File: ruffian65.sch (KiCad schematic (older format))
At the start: 23 parts

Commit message: wired differential
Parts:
- removed R? (x2): 22, symbol Device:R_Small
- removed U?: ATmega32U4-AU, Package_QFP:TQFP-44_10x10mm_P0.8mm, symbol MCU_Microchip_ATmega:ATmega32U4-AU
- added U1: ATmega32U4-MU, Package_DFN_QFN:QFN-44-1EP_7x7mm_P0.5mm_EP5.2x5.2mm, symbol MCU_Microchip_ATmega:ATmega32U4-MU
- C1, C2, C3, C4, C5, C7: footprint (none) -> Capacitor_SMD:C_0805_2012Metric_Pad1.18x1.45mm_HandSolder
- C6, C8: renamed from C?; footprint (none) -> Capacitor_SMD:C_0805_2012Metric_Pad1.18x1.45mm_HandSolder
- D70: renamed from D?; footprint Package_TO_SOT_SMD:SOT-143 -> random-keyboard-parts:SOT143B
- F1: renamed from F?; footprint (none) -> Fuse:Fuse_1206_3216Metric_Pad1.42x1.75mm_HandSolder
- J1: renamed from J?; footprint (none) -> random-keyboard-parts:Reset_Pretty-Mask
- R1: footprint (none) -> Resistor_SMD:R_0805_2012Metric_Pad1.20x1.40mm_HandSolder
- R2, R3, R4, R5, R6: renamed from R?; footprint (none) -> Resistor_SMD:R_0805_2012Metric_Pad1.20x1.40mm_HandSolder
- SW70: renamed from SW?; footprint (none) -> Button_Switch_SMD:SW_SPST_SKQG_WithStem
- USB1: renamed from USB?; footprint (none) -> Type-C:HRO-TYPE-C-31-M-12-HandSoldering
- Y1: renamed from Y?; footprint (none) -> Crystal:Crystal_SMD_3225-4Pin_3.2x2.5mm_HandSoldering
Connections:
- net +5V: now also U1.14 (VCC), U1.2 (UVCC), U1.34 (VCC), U1.7 (VBUS)
- net D+: now also U1.4 (D+)
- net D-: now also U1.3 (D-)
- net GND: now also U1.5 (UGND)
- net MISO: now also U1.11 (PB3)
- net MOSI: now also U1.10 (PB2)
- net RESET: now also U1.13 (~RESET)
- net SCK: now also U1.9 (PB1)
- net XTAL1: now also U1.17 (XTAL1)
- net XTAL2: now also U1.16 (XTAL2)
- net at R1.2: now also U1.33 (~HWB~/PE2)
- net at C7.1: now also U1.6 (UCAP)
- net DN: now reaches D70.3 (I/O2), R3.2, USB1.5 (DN2), USB1.7 (DN1)
- net DP: now reaches D70.2 (I/O1), R4.2, USB1.6 (DP1), USB1.8 (DP2)
- new net: U1.15 (GND), U1.23 (GND), U1.35 (GND), U1.43 (GND), U1.45 (GND)
- new net: U1.24 (AVCC), U1.44 (AVCC)
- new net col0: U1.28 (PB4)
- new net col1: U1.29 (PB5)
- new net col10: U1.21 (PD3)
- new net col11: U1.22 (PD5)
- new net col12: U1.25 (PD4)
- new net col13: U1.26 (PD6)
- new net col14: U1.27 (PD7)
- new net col2: U1.30 (PB6)
- new net col3: U1.31 (PC6)
- new net col4: U1.32 (PC7)
- new net col5: U1.37 (PF6)
- new net col6: U1.36 (PF7)
- new net col7: U1.8 (PB0)
- new net col8: U1.19 (PD1)
- new net col9: U1.20 (PD2)
- new net row0: U1.1 (PE6)
- new net row1: U1.38 (PF5)
- new net row2: U1.41 (PF0)
- new net row3: U1.40 (PF1)
- new net row4: U1.39 (PF4)

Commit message: wiring done?
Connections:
- net +5V: now also U1.24 (AVCC), U1.44 (AVCC)
- net GND: now also U1.15 (GND), U1.23 (GND), U1.35 (GND), U1.43 (GND), U1.45 (GND)
- net col0: now also U1.20 (PD2); no longer U1.28 (PB4)
- net col1: now also U1.21 (PD3); no longer U1.29 (PB5)
- net col10: now also U1.18 (PD0); no longer U1.21 (PD3)
- net col11: now also U1.41 (PF0); no longer U1.22 (PD5)
- net col2: now also U1.22 (PD5); no longer U1.30 (PB6)
- net col8: now also U1.28 (PB4); no longer U1.19 (PD1)
- net col9: now also U1.38 (PF5); no longer U1.20 (PD2)
- net row1: now also U1.39 (PF4); no longer U1.38 (PF5)
- net row2: now also U1.12 (PB7); no longer U1.41 (PF0)
- net row4: now also U1.19 (PD1); no longer U1.39 (PF4)
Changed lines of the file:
@@
 Wire Wire Line
 	10750 3400 11050 3400
-Text GLabel 10250 1700 2    50   Input ~ 0
+Text GLabel 10250 2700 2    50   Input ~ 0
 col0
 Wire Wire Line
@@
 Wire Wire Line
 	10250 1600 10800 1600
-Text GLabel 10250 1800 2    50   Input ~ 0
+Text GLabel 10250 2800 2    50   Input ~ 0
 col1
-Text GLabel 10250 1900 2    50   Input ~ 0
+Text GLabel 10250 3000 2    50   Input ~ 0
 col2
 Text GLabel 10250 2300 2    50   Input ~ 0
@@
 col3
 Text GLabel 10250 2600 2    50   Input ~ 0
-col8
-Text GLabel 10250 2700 2    50   Input ~ 0
+row4
+Text GLabel 10250 4000 2    50   Input ~ 0
 col9
-Text GLabel 10250 2800 2    50   Input ~ 0
+Text GLabel 10250 2500 2    50   Input ~ 0
 col10
-Text GLabel 10250 3000 2    50   Input ~ 0
+Text GLabel 10250 3700 2    50   Input ~ 0
 col11
 Text GLabel 10250 2900 2    50   Input ~ 0
@@
 Text GLabel 10250 3500 2    50   Input ~ 0
 row0
-Text GLabel 10250 4000 2    50   Input ~ 0
+Text GLabel 10250 3900 2    50   Input ~ 0
 row1
-Text GLabel 10250 3700 2    50   Input ~ 0
+Text GLabel 10250 2000 2    50   Input ~ 0
 row2
 Text GLabel 10250 3800 2    50   Input ~ 0
 row3
-Text GLabel 10250 3900 2    50   Input ~ 0
-row4
+Text GLabel 10250 1700 2    50   Input ~ 0
+col8
 Text GLabel 10250 4100 2    50   Input ~ 0
 col5
 Text GLabel 10250 4200 2    50   Input ~ 0
 col6
+Wire Wire Line
+	9150 4600 9550 4600
+Wire Wire Line
+	9550 1000 9650 1000
+Text GLabel 6450 3400 3    50   Input ~ 0
+DP
+Text GLabel 6450 3300 1    50   Input ~ 0
+DN
 $Comp
 L MCU_Microchip_ATmega:ATmega32U4-MU U1
-U 1 1 61957B02
+U 1 1 61B499E8
 P 9650 2800
 F 0 "U1" H 9650 911 50  0000 C CNN
@@
 	1    0    0    -1
 $EndComp
+Connection ~ 9550 1000
 Wire Wire Line
-	9150 4600 9550 4600
+	9750 1000 9650 1000
+Connection ~ 9650 1000
 Wire Wire Line
-	9550 1000 9650 1000
-Connection ~ 9550 1000
-Text GLabel 6450 3400 3    50   Input ~ 0
-DP
-Text GLabel 6450 3300 1    50   Input ~ 0
-DN
+	9650 4600 9550 4600
+Connection ~ 9550 4600
 $EndSCHEMATC

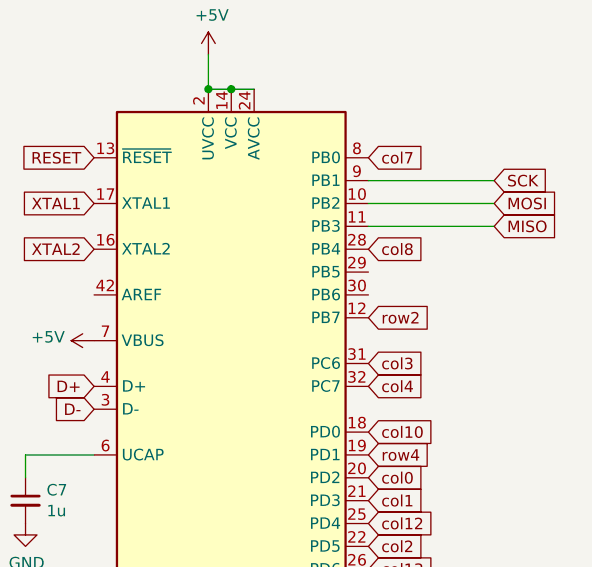
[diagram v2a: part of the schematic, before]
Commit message: added ec11
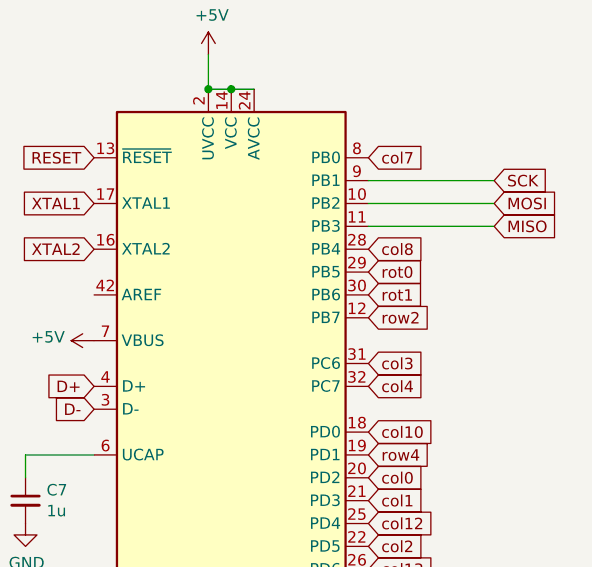
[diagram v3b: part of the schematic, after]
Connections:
- net rot0: now reaches U1.29 (PB5)
- net rot1: now reaches U1.30 (PB6)
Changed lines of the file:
@@
 	9650 4600 9550 4600
 Connection ~ 9550 4600
+Text GLabel 10250 1800 2    50   Input ~ 0
+rot0
+Text GLabel 10250 1900 2    50   Input ~ 0
+rot1
 $EndSCHEMATC

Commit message: encoder support?
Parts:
- removed USB1: HRO-TYPE-C-31-M-12, Type-C:HRO-TYPE-C-31-M-12-HandSoldering, symbol Type-C:HRO-TYPE-C-31-M-12
- added J2: USB_C_Receptacle_USB2.0, Connector_USB:USB_C_Receptacle_HRO_TYPE-C-31-M-12, symbol Connector:USB_C_Receptacle_USB2.0
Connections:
- net DN: now also J2.A7 (D-), J2.B7 (D-)
- net DP: now also J2.A6 (D+), J2.B6 (D+)
- net GND: now also J2.A1 (GND), J2.A12 (GND), J2.B1 (GND), J2.B12 (GND), J2.S1 (SHIELD)
- net VCC: now also J2.A4 (VBUS), J2.A9 (VBUS), J2.B4 (VBUS), J2.B9 (VBUS)
- net at R5.1: now also J2.B5 (CC2)
- net at R6.1: now also J2.A5 (CC1)
- no-connect marks 0 -> 2
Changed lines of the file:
@@
 	7200 1500 7200 1650
-$Comp
-L Type-C:HRO-TYPE-C-31-M-12 USB1
-U 1 1 6139D968
-P 5800 3250
-F 0 "USB1" H 5633 4047 60  0000 C CNN
-F 1 "HRO-TYPE-C-31-M-12" H 5633 3941 60  0000 C CNN
-F 2 "Type-C:HRO-TYPE-C-31-M-12-HandSoldering" H 5800 3250 60  0001 C CNN
-F 3 "" H 5800 3250 60  0001 C CNN
-	1    5800 3250
-	1    0    0    -1
-$EndComp
 $Comp
 L Device:R_Small R3
@@
 Wire Wire Line
 	7900 3400 8150 3400
-Wire Wire Line
-	5900 2700 6000 2700
-Wire Wire Line
-	6000 2700 6000 3800
-Wire Wire Line
-	6000 3800 5900 3800
-Wire Wire Line
-	5900 3900 6000 3900
-Wire Wire Line
-	6000 3900 6000 3800
-Connection ~ 6000 3800
 $Comp
 L power:VCC #PWR0112
@@
 	1    0    0    -1
 $EndComp
-Wire Wire Line
-	5900 2800 6100 2800
-Wire Wire Line
-	5900 3400 6200 3400
-Wire Wire Line
-	5900 3300 6300 3300
-Wire Wire Line
-	5900 3100 6300 3100
-Wire Wire Line
-	6300 3100 6300 3300
-Wire Wire Line
-	5900 3200 6200 3200
-Wire Wire Line
-	6200 3200 6200 3400
-Wire Wire Line
-	5900 3700 6100 3700
-Wire Wire Line
-	6100 3700 6100 2800
-Connection ~ 6100 2800
-Wire Wire Line
-	6100 2800 6600 2800
 $Comp
 L Device:Polyfuse_Small F1
@@
 $EndComp
 Wire Wire Line
-	5900 3600 6450 3600
-Wire Wire Line
-	6000 3800 6150 3800
-Wire Wire Line
 	6450 3800 6650 3800
 Connection ~ 6450 3800
@@
 Wire Wire Line
 	6150 3800 6450 3800
-Wire Wire Line
-	6300 3300 6950 3300
-Connection ~ 6300 3300
-Wire Wire Line
-	6200 3400 7450 3400
-Connection ~ 6200 3400
 $Comp
 L Power_Protection:PRTR5V0U2X D70
@@
 Text GLabel 10250 1900 2    50   Input ~ 0
 rot1
+$Comp
+L Connector:USB_C_Receptacle_USB2.0 J2
+U 1 1 613F3603
+P 4100 3300
+F 0 "J2" H 4207 4167 50  0000 C CNN
+F 1 "USB_C_Receptacle_USB2.0" H 4207 4076 50  0000 C CNN
+F 2 "Connector_USB:USB_C_Receptacle_HRO_TYPE-C-31-M-12" H 4250 3300 50  0001 C CNN
+F 3 "https://www.usb.org/sites/default/files/documents/usb_type-c.zip" H 4250 3300 50  0001 C CNN
+	1    4100 3300
+	1    0    0    -1
+$EndComp
+Wire Wire Line
+	5900 3600 6450 3600
+NoConn ~ 4700 3900
+NoConn ~ 4700 3800
+Wire Wire Line
+	4700 3500 4700 3400
+Connection ~ 4700 3400
+Wire Wire Line
+	4700 3300 4700 3200
+Connection ~ 4700 3300
+Wire Wire Line
+	4700 3400 7450 3400
+Wire Wire Line
+	4700 3300 6950 3300
+Wire Wire Line
+	4100 4200 5900 4200
+Wire Wire Line
+	5900 3800 5900 4200
+Wire Wire Line
+	5900 3800 6150 3800
+Wire Wire Line
+	4700 2700 5900 2700
+Wire Wire Line
+	5900 2700 5900 2800
+Wire Wire Line
+	4700 2900 5900 2900
+Wire Wire Line
+	5900 2900 5900 3000
+Wire Wire Line
+	4700 3000 5050 3000
+Wire Wire Line
+	5050 3000 5050 3250
+Wire Wire Line
+	5050 3250 5900 3250
+Wire Wire Line
+	5900 3250 5900 3600
+Wire Wire Line
+	5900 2800 6600 2800
+Wire Wire Line
+	3800 4200 4100 4200
+Connection ~ 4100 4200
 $EndSCHEMATC
